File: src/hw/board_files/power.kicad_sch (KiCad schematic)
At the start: 25 parts, among them J1 USB_C_Receptacle_USB2.0_14P, J2 Conn_01x03, U1 TLV62569DBV, U2 USBLC6-2SC6, U3 MCP73871

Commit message: Schematic done. Started layout
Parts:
- removed J1: USB_C_Receptacle_USB2.0_14P, Connector_USB:USB_C_Receptacle_GCT_USB4105-xx-A_16P_TopMnt_Horizontal, symbol Connector:USB_C_Receptacle_USB2.0_14P
- added J1: USB_C_Receptacle_USB2.0_16P, Connector_USB:USB_C_Receptacle_GCT_USB4105-xx-A_16P_TopMnt_Horizontal, symbol Connector:USB_C_Receptacle_USB2.0_16P
- FB1: value FerriteBead -> BLM21PG221SN1D; footprint (none) -> Inductor_SMD:L_0805_2012Metric_Pad1.05x1.20mm_HandSolder
- J2: footprint (none) -> Connector_PinSocket_2.54mm:PinSocket_1x03_P2.54mm_Horizontal
- L1: footprint Inductor_SMD:L_Bourns_SRN6045TA -> Inductor_SMD:L_Bourns-SRN4018; MPN (none) -> SRN4018-2R2M
- R1, R3, R4, R5: footprint (none) -> Resistor_SMD:R_0603_1608Metric_Pad0.98x0.95mm_HandSolder
- R2, R6: footprint (none) -> Resistor_SMD:R_0805_2012Metric_Pad1.20x1.40mm_HandSolder
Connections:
- net GND: now also J1.A1 (GND), J1.A12 (GND), J1.B1 (GND), J1.B12 (GND), J1.S1 (SHIELD)
- net at U2.1 (I/O1): now also J1.A7 (D-), J1.B7 (D-)
- net at U2.3 (I/O2): now also J1.A6 (D+), J1.B6 (D+)
- net at FB1.1: now also J1.A4 (VBUS), J1.A9 (VBUS), J1.B4 (VBUS), J1.B9 (VBUS)
- net at R5.1: now also J1.A5 (CC1)
- net at R4.1: now also J1.B5 (CC2)
- no-connect marks 0 -> 2
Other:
- note removed: "Find alternative to XAL4020-222ME for L3"
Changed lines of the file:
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@@
 		)
 	)
-	(text "Find alternative to XAL4020-222ME for L3"
-		(exclude_from_sim no)
-		(at 204.216 41.402 0)
-		(effects
-			(font
-				(size 1.27 1.27)
-			)
-		)
-	)
 	(text "Power"
 		(exclude_from_sim no)
@@
 		(color 0 0 0 0)
 	)
+	(no_connect
+		(at 54.61 69.85)
+	)
+	(no_connect
+		(at 54.61 72.39)
+	)
 	(wire
 		(pts
@@
 	)
 	(symbol
-		(lib_id "Connector:USB_C_Receptacle_USB2.0_14P")
-		(at 39.37 57.15 0)
-		(unit 1)
-		(exclude_from_sim no)
-		(in_bom yes)
-		(on_board yes)
-		(dnp no)
-		(fields_autoplaced yes)
-		(property "Reference" "J1"
-			(at 39.37 34.29 0)
-			(effects
-				(font
-					(size 1.27 1.27)
-				)
-			)
-		)
-		(property "Value" "USB_C_Receptacle_USB2.0_14P"
-			(at 39.37 36.83 0)
-			(effects
-				(font
-					(size 1.27 1.27)
-				)
-			)
-		)
-		(property "Footprint" "Connector_USB:USB_C_Receptacle_GCT_USB4105-xx-A_16P_TopMnt_Horizontal"
-			(at 43.18 57.15 0)
-			(effects
-				(font
-					(size 1.27 1.27)
-				)
-				(hide yes)
-			)
-		)
-		(property "Datasheet" "https://www.usb.org/sites/default/files/documents/usb_type-c.zip"
-			(at 43.18 57.15 0)
-			(effects
-				(font
-					(size 1.27 1.27)
-				)
-				(hide yes)
-			)
-		)
-		(property "Description" "USB 2.0-only 14P Type-C Receptacle connector"
-			(at 39.37 57.15 0)
-			(effects
-				(font
-					(size 1.27 1.27)
-				)
-				(hide yes)
-			)
-		)
-		(pin "A7"
-		)
-		(pin "B7"
-		)
-		(pin "S1"
-		)
-		(pin "A4"
-		)
-		(pin "B9"
-		)
-		(pin "B5"
-		)
-		(pin "B12"
-		)
-		(pin "B4"
-		)
-		(pin "A5"
-		)
-		(pin "A9"
-		)
-		(pin "A6"
-		)
-		(pin "B6"
-		)
-		(pin "A12"
-		)
-		(pin "B1"
-		)
-		(pin "A1"
-		)
-		(instances
-			(project "e-ink-picture-frame"
-				(path "/a2fcbc2d-b484-416d-9c38-bf03776db98a/89315c17-e1a8-43ce-82fd-dd881e7cfdc7"
-					(reference "J1")
-					(unit 1)
-				)
-			)
-		)
-	)
-	(symbol
 		(lib_id "Device:R_Small_US")
 		(at 222.25 67.31 0)
@@
 			)
 		)
-		(property "Footprint" ""
+		(property "Footprint" "Resistor_SMD:R_0805_2012Metric_Pad1.20x1.40mm_HandSolder"
 			(at 222.25 67.31 0)
 			(effects
@@
 			)
 		)
-		(property "Footprint" "Inductor_SMD:L_Bourns_SRN6045TA"
+		(property "Footprint" "Inductor_SMD:L_Bourns-SRN4018"
 			(at 204.47 52.07 0)
 			(effects
@@
 			)
 		)
+		(property "MPN" "SRN4018-2R2M"
+			(at 204.47 52.07 90)
+			(effects
+				(font
+					(size 1.27 1.27)
+				)
+				(hide yes)
+			)
+		)
+		(property "Mouser PN" ""
+			(at 204.47 52.07 90)
+			(effects
+				(font
+					(size 1.27 1.27)
+				)
+				(hide yes)
+			)
+		)
 		(pin "2"
 		)
@@
 			)
 		)
-		(property "Footprint" ""
+		(property "Footprint" "Resistor_SMD:R_0603_1608Metric_Pad0.98x0.95mm_HandSolder"
 			(at 67.31 67.31 0)
 			(effects
@@
 	)
 	(symbol
+		(lib_id "Connector:USB_C_Receptacle_USB2.0_16P")
+		(at 39.37 57.15 0)
+		(unit 1)
+		(exclude_from_sim no)
+		(in_bom yes)
+		(on_board yes)
+		(dnp no)
+		(fields_autoplaced yes)
+		(property "Reference" "J1"
+			(at 39.37 34.29 0)
+			(effects
+				(font
+					(size 1.27 1.27)
+				)
+			)
+		)
+		(property "Value" "USB_C_Receptacle_USB2.0_16P"
+			(at 39.37 36.83 0)
+			(effects
+				(font
+					(size 1.27 1.27)
+				)
+			)
+		)
+		(property "Footprint" "Connector_USB:USB_C_Receptacle_GCT_USB4105-xx-A_16P_TopMnt_Horizontal"
+			(at 43.18 57.15 0)
+			(effects
+				(font
+					(size 1.27 1.27)
+				)
+				(hide yes)
+			)
+		)
+		(property "Datasheet" "https://www.usb.org/sites/default/files/documents/usb_type-c.zip"
+			(at 43.18 57.15 0)
+			(effects
+				(font
+					(size 1.27 1.27)
+				)
+				(hide yes)
+			)
+		)
+		(property "Description" "USB 2.0-only 16P Type-C Receptacle connector"
+			(at 39.37 57.15 0)
+			(effects
+				(font
+					(size 1.27 1.27)
+				)
+				(hide yes)
+			)
+		)
+		(pin "B12"
+		)
+		(pin "B7"
+		)
+		(pin "A1"
+		)
+		(pin "A9"
+		)
+		(pin "B9"
+		)
+		(pin "A7"
+		)
+		(pin "A12"
+		)
+		(pin "B1"
+		)
+		(pin "B8"
+		)
+		(pin "S1"
+		)
+		(pin "A4"
+		)
+		(pin "B4"
+		)
+		(pin "A6"
+		)
+		(pin "A5"
+		)
+		(pin "B5"
+		)
+		(pin "B6"
+		)
+		(pin "A8"
+		)
+		(instances
+			(project ""
+				(path "/a2fcbc2d-b484-416d-9c38-bf03776db98a/89315c17-e1a8-43ce-82fd-dd881e7cfdc7"
+					(reference "J1")
+					(unit 1)
+				)
+			)
+		)
+	)
+	(symbol
 		(lib_id "Device:C_Small")
 		(at 132.08 134.62 0)
@@
 			)
 		)
-		(property "Footprint" ""
+		(property "Footprint" "Resistor_SMD:R_0603_1608Metric_Pad0.98x0.95mm_HandSolder"
 			(at 97.79 59.69 0)
 			(effects
@@
 			)
 		)
-		(property "Footprint" ""
+		(property "Footprint" "Resistor_SMD:R_0603_1608Metric_Pad0.98x0.95mm_HandSolder"
 			(at 97.79 57.15 0)
 			(effects
@@
 			)
 		)
-		(property "Footprint" ""
+		(property "Footprint" "Resistor_SMD:R_0603_1608Metric_Pad0.98x0.95mm_HandSolder"
 			(at 62.23 67.31 0)
 			(effects
@@
 		(exclude_from_sim no)
 		(in_bom yes)
-		(on_board yes)
+		(on_board no)
 		(dnp no)
 		(fields_autoplaced yes)
@@
 			)
 		)
-		(property "Footprint" ""
+		(property "Footprint" "Connector_PinSocket_2.54mm:PinSocket_1x03_P2.54mm_Horizontal"
 			(at 172.72 132.08 0)
 			(effects
@@
 			)
 		)
-		(property "Footprint" ""
+		(property "Footprint" "Resistor_SMD:R_0805_2012Metric_Pad1.20x1.40mm_HandSolder"
 			(at 222.25 57.15 0)
 			(effects
@@
 			)
 		)
-		(property "Value" "FerriteBead"
+		(property "Value" "BLM21PG221SN1D"
 			(at 64.7192 36.83 90)
 			(effects
@@
 			)
 		)
-		(property "Footprint" ""
+		(property "Footprint" "Inductor_SMD:L_0805_2012Metric_Pad1.05x1.20mm_HandSolder"
 			(at 64.77 43.688 90)
 			(effects

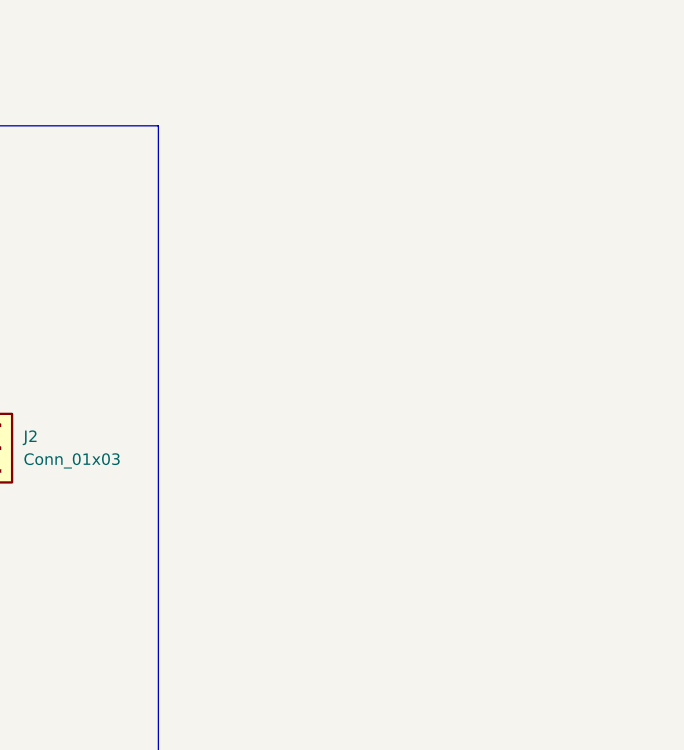
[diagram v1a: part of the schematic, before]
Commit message: Laid out main components
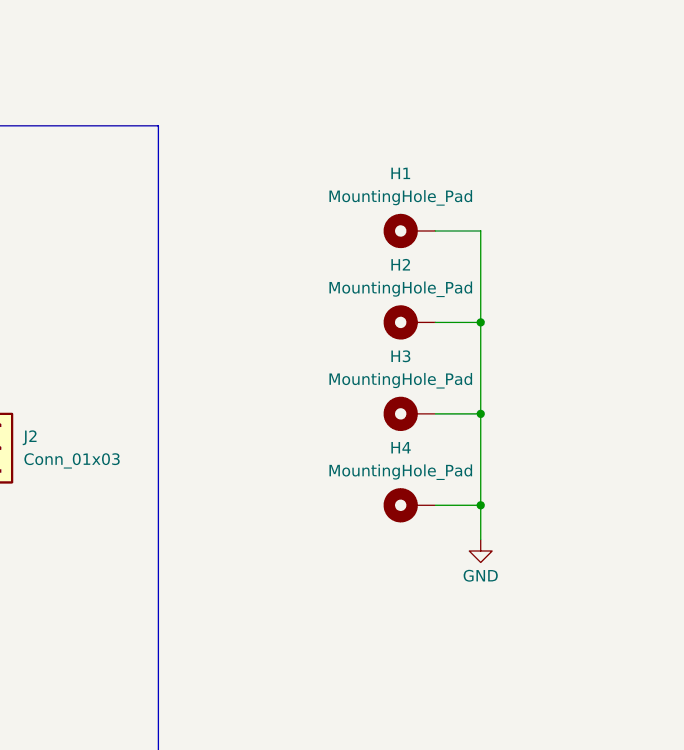
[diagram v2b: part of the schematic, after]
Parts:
- added H1, H2, H3, H4: MountingHole_Pad, MountingHole:MountingHole_3.2mm_M3_Pad, symbol Mechanical:MountingHole_Pad
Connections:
- net GND: now also H1.1, H2.1, H3.1, H4.1
